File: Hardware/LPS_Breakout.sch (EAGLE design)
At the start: 11 parts

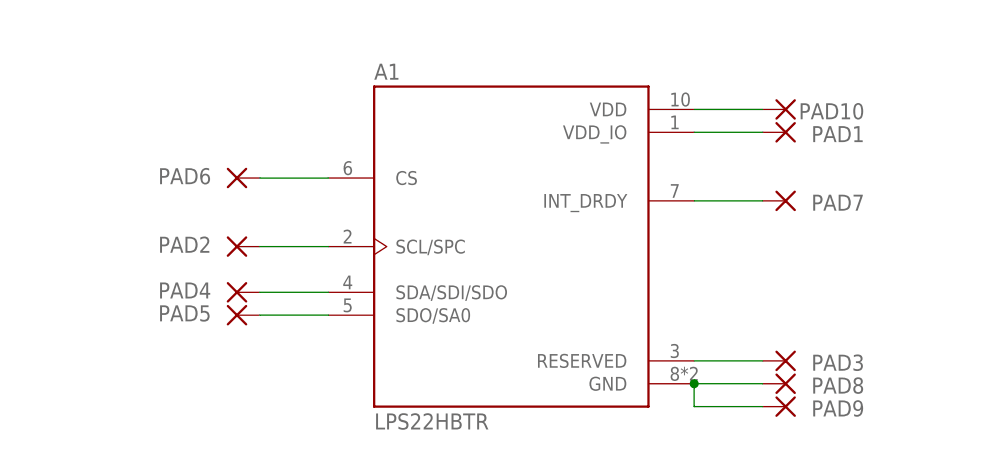
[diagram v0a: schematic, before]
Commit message: updated pinheaders and names
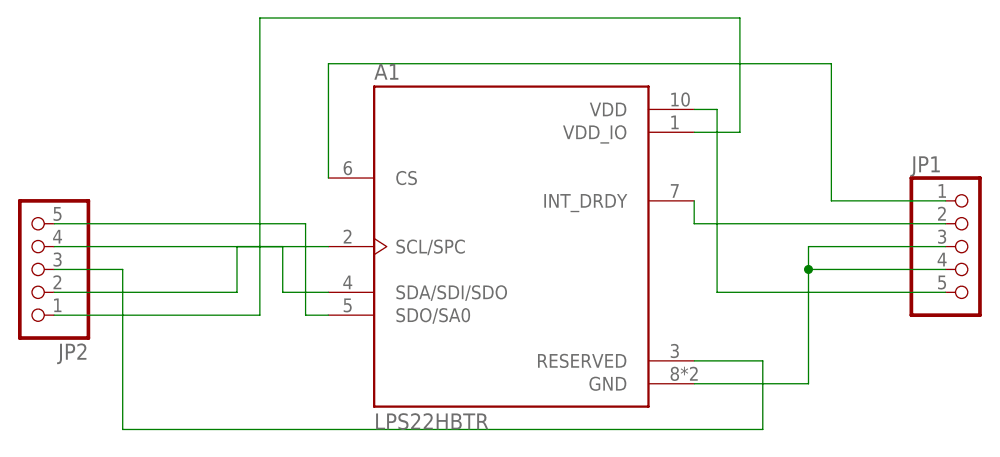
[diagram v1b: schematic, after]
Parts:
- removed PAD1, PAD10, PAD2, PAD3, PAD4, PAD5, PAD6, PAD7, PAD8, PAD9: (no value), wirepad:1,6/0,8
- added JP1, JP2: (no value), pinhead:PINHD-1X5
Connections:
- removed net N$7: A1.INT_DRDY, PAD7.P
- new net N$9: A1.GND, JP1.3, JP1.4
- net N$1: now also JP2.1; no longer PAD1.P
- net N$10: now also JP1.5; no longer PAD10.P
- net N$2: now also JP2.2; no longer PAD2.P
- net N$3: now also JP2.3; no longer PAD3.P
- net N$4: now also JP2.4; no longer PAD4.P
- net N$5: now also JP2.5; no longer PAD5.P
- net N$6: now also JP1.1; no longer PAD6.P
- net N$8: now also A1.INT_DRDY, JP1.2; no longer A1.GND, PAD8.P, PAD9.P
